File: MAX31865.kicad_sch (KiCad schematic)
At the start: 25 parts, among them U1 MAX31865, U2 MIC5225-3.3, X1 3.5mm, X2 3.5mm

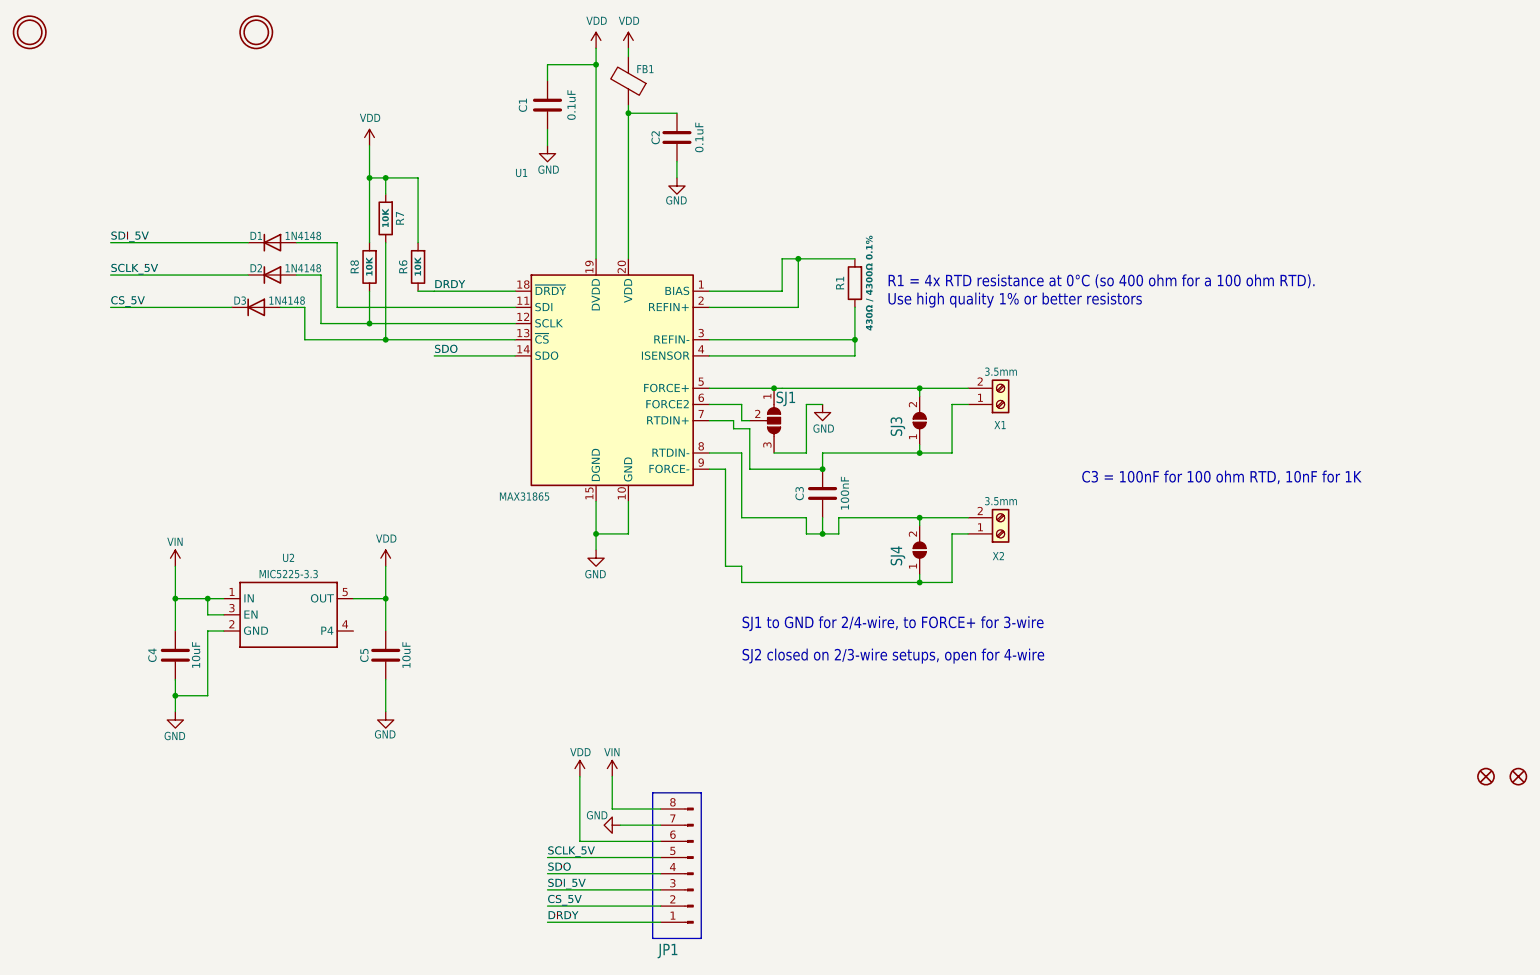
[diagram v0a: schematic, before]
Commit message: fixed routing + added BOM info
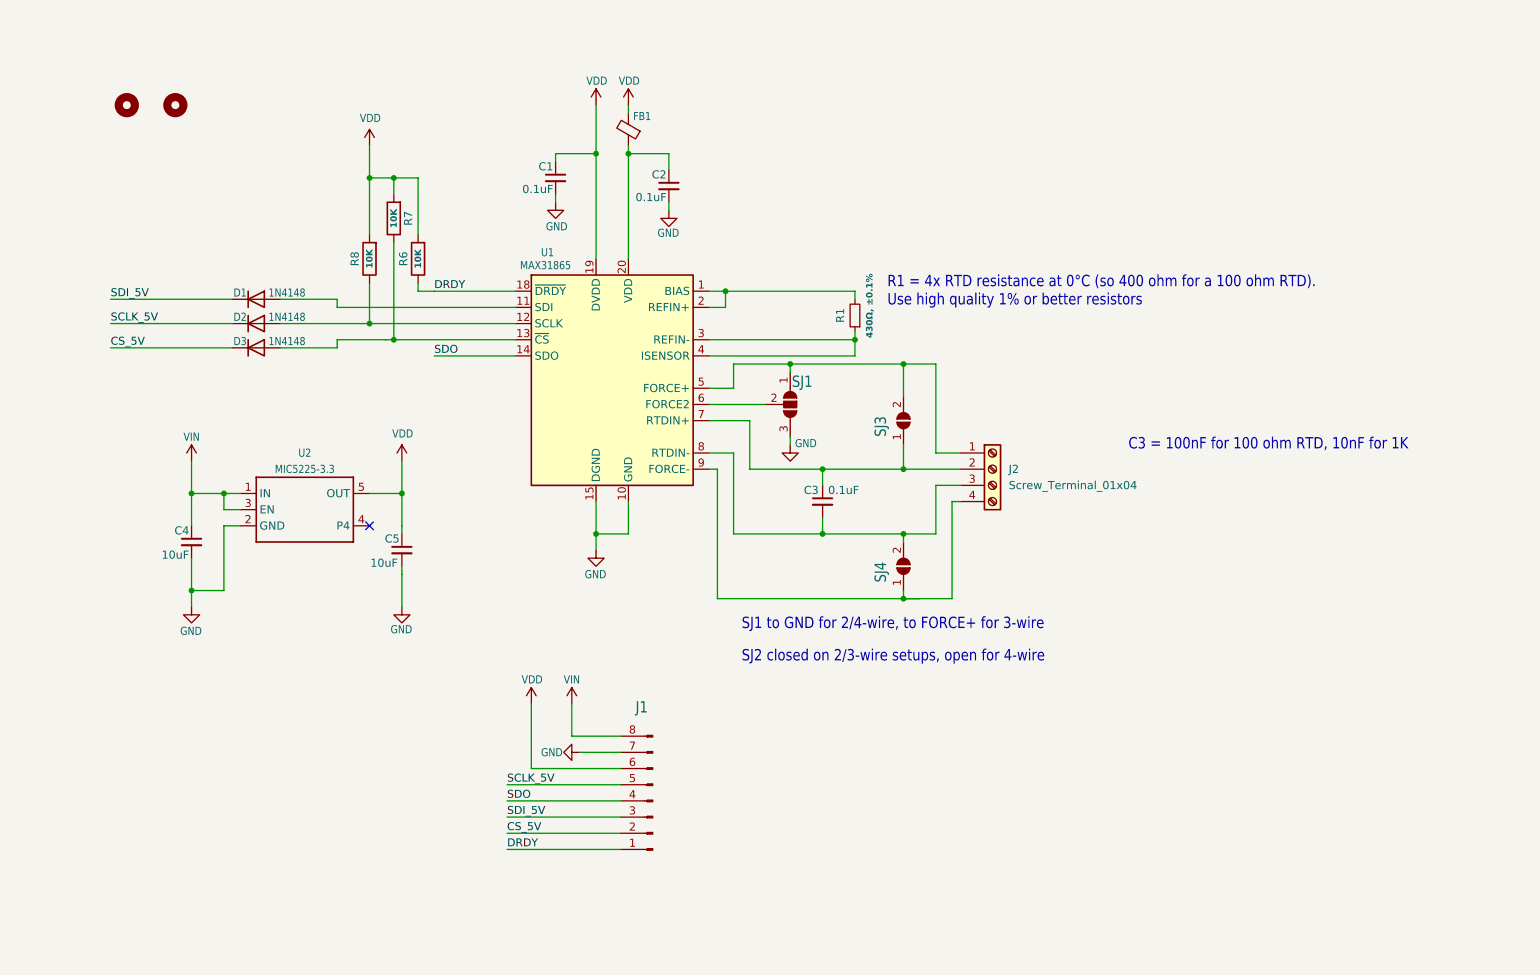
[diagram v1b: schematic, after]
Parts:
- removed FID1, FID2: FIDUCIAL{dblquote}{dblquote}, Fiducial:Fiducial_1mm_Mask2mm, symbol MAX31865-eagle-import:FIDUCIAL{dblquote}{dblquote}
- removed X1, X2: 3.5mm, TerminalBlock_4Ucon:TerminalBlock_4Ucon_1x02_P3.50mm_Horizontal, symbol Connector:Screw_Terminal_01x02
- added J2: Screw_Terminal_01x04, TerminalBlock_4Ucon:TerminalBlock_4Ucon_1x04_P3.50mm_Horizontal, symbol Connector:Screw_Terminal_01x04
- C1, C2: symbol Device:C -> Device:C_Small; MPN (none) -> /; Manufacturer (none) -> /; SPN (none) -> GPC0805104; Supplier (none) -> Eurocircuits
- C3: value 100nF -> 0.1uF; symbol Device:C -> Device:C_Small; MPN (none) -> /; Manufacturer (none) -> /; SPN (none) -> GPC0805104; Supplier (none) -> Eurocircuits
- C4, C5: symbol Device:C -> Device:C_Small; Component package type (none) -> C_0805; MPN (none) -> /; Manufacturer (none) -> /; SPN (none) -> GPC0805106-16; Supplier (none) -> Eurocircuits
- D1, D2, D3: Component package type (none) -> SOD-323; MPN (none) -> 1N4148WX-TP; Manufacturer (none) -> Micro Commercial Co; SPN (none) -> 1N4148WXTPMSTR-ND; Supplier (none) -> DigiKey
- FB1: footprint MAX31865:0805-NO -> Inductor_SMD:L_0805_2012Metric; symbol Device:FerriteBead -> Device:FerriteBead_Small; MPN (none) -> LI0805G201R-10; Manufacturer (none) -> Laird-Signal Integrity Products; SPN (none) -> 240-2549-2-ND; Supplier (none) -> DigiKey
- J1: renamed from JP1; value HEADER-1X870MIL -> connector; footprint Connector_PinHeader_1.00mm:PinHeader_1x08_P1.00mm_Vertical -> Connector_PinHeader_2.54mm:PinHeader_1x08_P2.54mm_Vertical; Component package type (none) -> /; MPN (none) -> TSW-108-09-G-S; Manufacturer (none) -> Samtec Inc.; SPN (none) -> SAM12332-ND; Supplier (none) -> DigiKey
- R1: value 430Ω / 4300Ω 0.1% -> 430Ω, ±0.1%; symbol Device:R -> Device:R_Small; MPN (none) -> /; Manufacturer (none) -> /; SPN (none) -> GPR0805430R; Supplier (none) -> Eurocircuits
- R6, R7, R8: MPN (none) -> /; Manufacturer (none) -> /; SPN (none) -> GPR080510K; Supplier (none) -> Eurocircuits
- SJ1: footprint MAX31865:SOLDERJUMPER_2WAY_OPEN_NOPASTE -> Jumper:SolderJumper-3_P1.3mm_Open_Pad1.0x1.5mm; now left out of the parts list
- SJ3, SJ4: now left out of the parts list
- U$18, U$19: footprint MountingHole:MountingHole_2.5mm -> MountingHole:MountingHole_2.2mm_M2_ISO7380; symbol MAX31865-eagle-import:MOUNTINGHOLE2.5 -> Mechanical:MountingHole; now left out of the parts list
- U1: Component package type (none) -> 20-TQFN (5x5); MPN (none) -> MAX31865ATP+; Manufacturer (none) -> Analog Devices Inc./Maxim Integrated; SPN (none) -> MAX31865ATP+-ND; Supplier (none) -> DigiKey
- U2: Component package type (none) -> SOT-235; MPN (none) -> MIC5225-3.3YM5-TR; Manufacturer (none) -> Microchip Technology; SPN (none) -> 576-2980-2-ND; Supplier (none) -> DigiKey
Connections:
- net at SJ4.1 (A), U1.9 (FORCE-): now also J2.4 (Pin_4)
- net at C3.2, SJ4.2 (B), U1.8 (RTDIN-): now also J2.3 (Pin_3)
- net at C3.1, SJ3.1 (A), U1.7 (RTDIN+): now also J2.2 (Pin_2)
- net at SJ1.1 (A), SJ3.2 (B), U1.5 (FORCE+): now also J2.1 (Pin_1)
- no-connect marks 0 -> 1
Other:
- moved on the sheet: C1, C2, C3, C4, C5, D1, D2, D3, FB1, J1, R1, R6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

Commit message: removed imported library
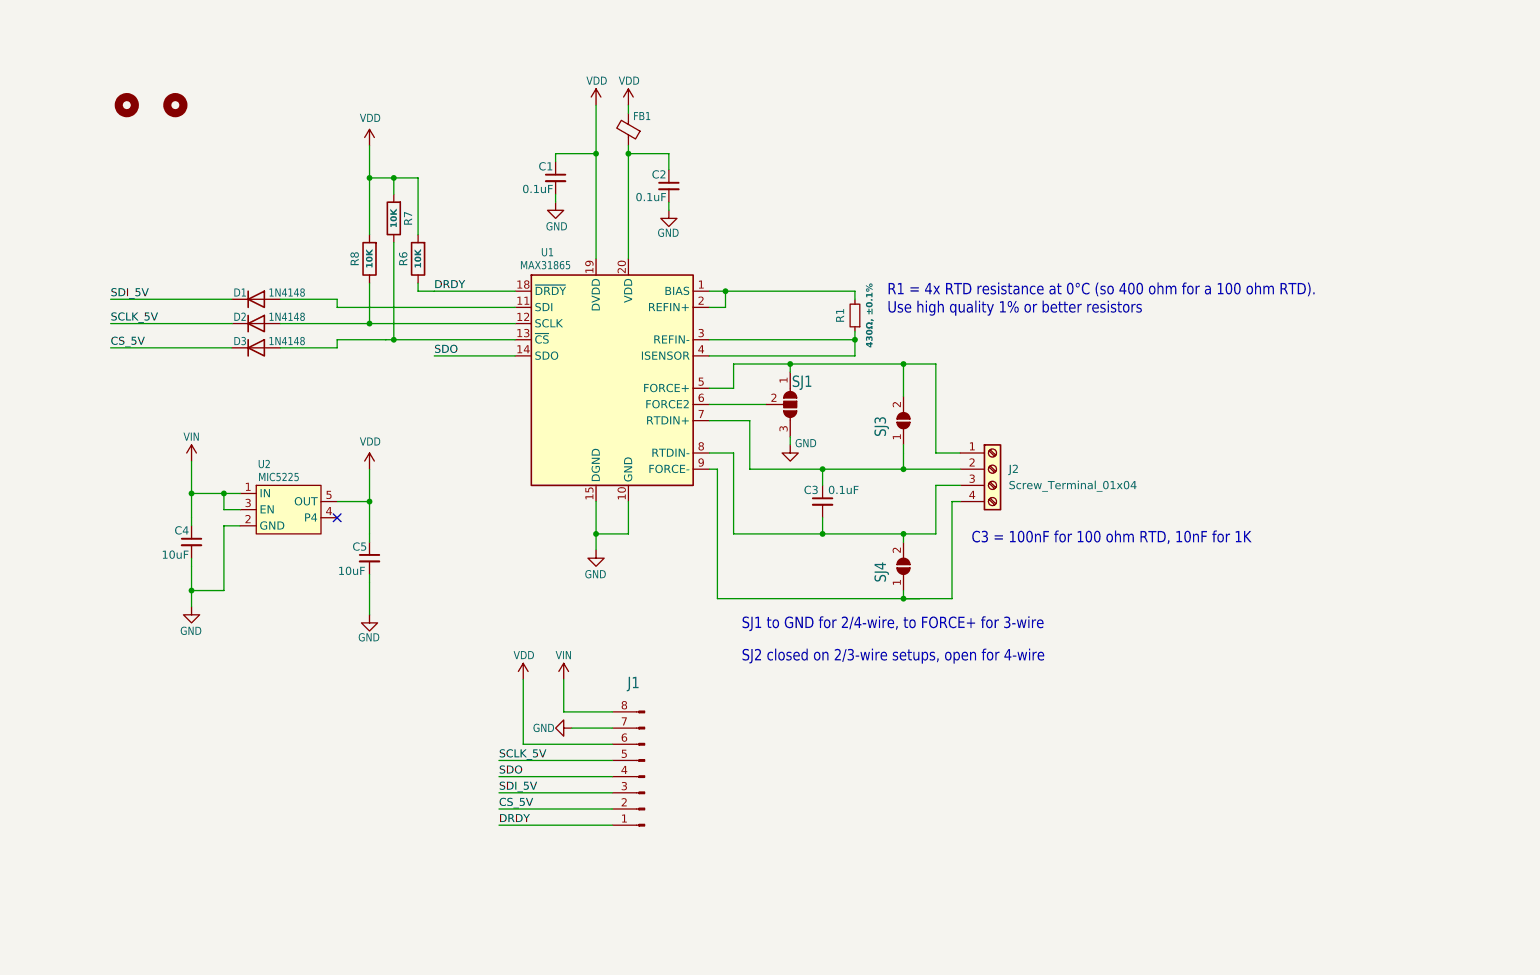
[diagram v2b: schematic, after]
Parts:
- U2: value MIC5225-3.3 -> MIC5225; symbol VREG_SOT23-5:VREG_SOT23-5 -> external_library:MIC5225
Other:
- moved on the sheet: C5, J1

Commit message: improved routing
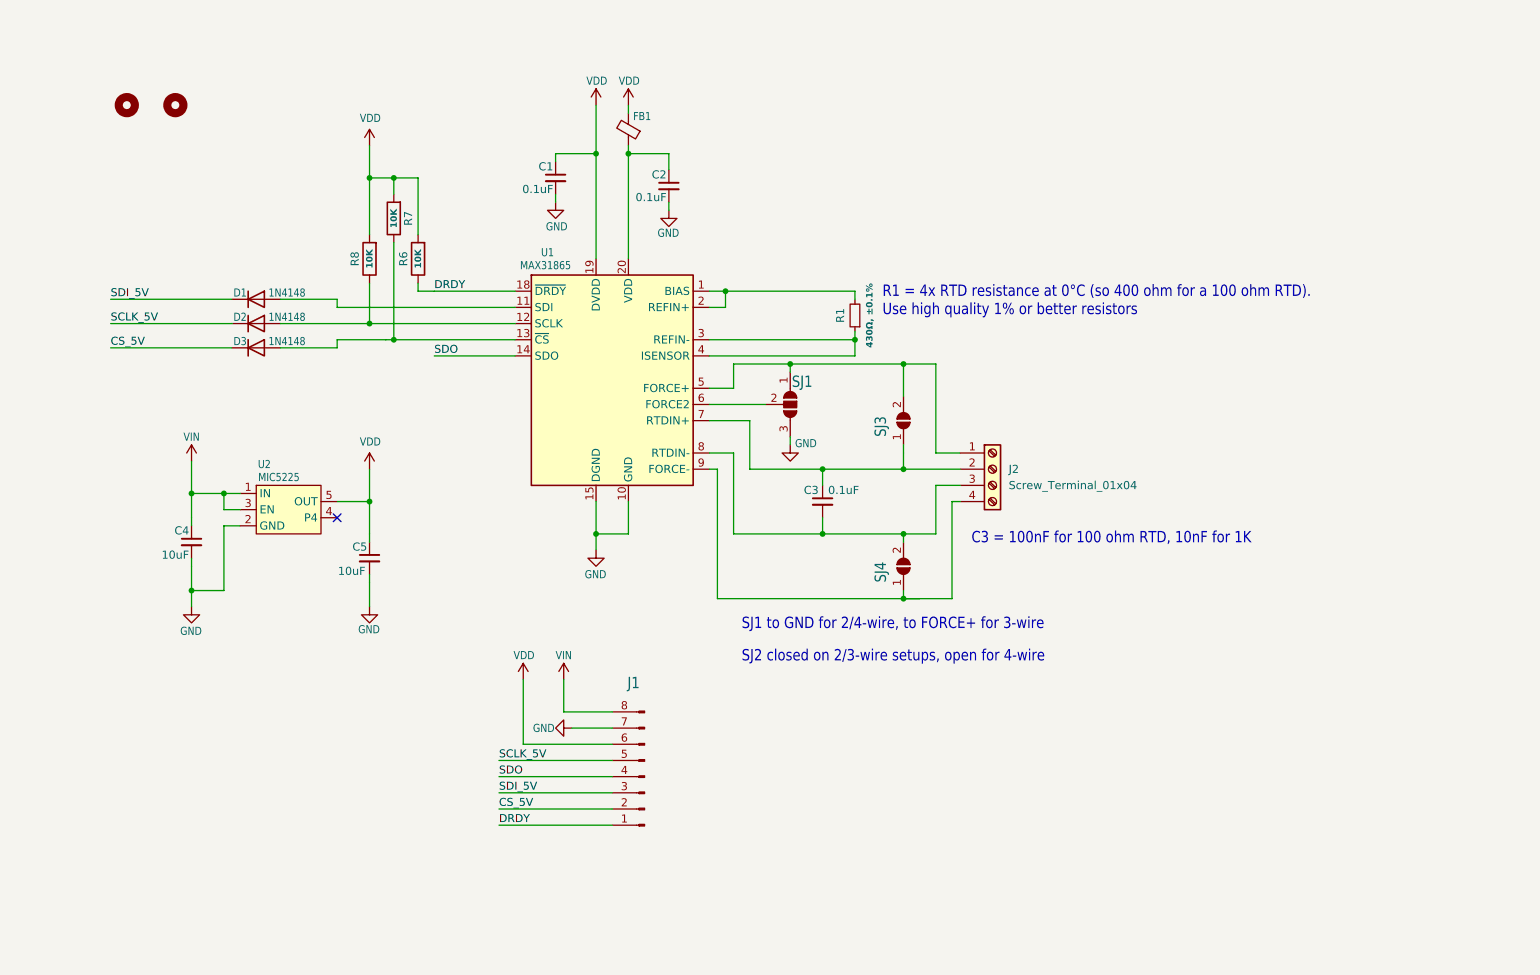
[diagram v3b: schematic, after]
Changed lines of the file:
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@@
 	(wire
 		(pts
-			(xy 91.44 127) (xy 91.44 132.08)
+			(xy 91.44 127) (xy 91.44 130.81)
 		)
 		(stroke
@@
 	(text "R1 = 4x RTD resistance at 0°C (so 400 ohm for a 100 ohm RTD).\nUse high quality 1% or better resistors"
 		(exclude_from_sim no)
-		(at 172.72 85.09 0)
+		(at 171.958 85.344 0)
 		(effects
 			(font
@@
 	(symbol
 		(lib_id "power:GND")
-		(at 91.44 132.08 0)
+		(at 91.44 130.81 0)
 		(unit 1)
 		(exclude_from_sim no)
@@
 		(dnp no)
 		(property "Reference" "#U$012"
-			(at 91.44 132.08 0)
+			(at 91.44 130.81 0)
 			(effects
 				(font
@@
 		)
 		(property "Value" "GND"
-			(at 89.662 136.398 0)
+			(at 89.662 135.128 0)
 			(effects
 				(font
@@
 		)
 		(property "Footprint" ""
-			(at 91.44 132.08 0)
+			(at 91.44 130.81 0)
 			(effects
 				(font
@@
 		)
 		(property "Datasheet" ""
-			(at 91.44 132.08 0)
+			(at 91.44 130.81 0)
 			(effects
 				(font
@@
 		)
 		(property "Description" "Power symbol creates a global label with name \"GND\" , ground"
-			(at 91.44 132.08 0)
-			(effects
-				(font
+			(at 91.44 130.81 0)
+			(effects
+				(font

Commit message: updated solder jumper
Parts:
- removed SJ1: SOLDERJUMPER_2WAY, Jumper:SolderJumper-3_P1.3mm_Open_Pad1.0x1.5mm, symbol Jumper:SolderJumper_3_Open
- added JP1: SolderJumper_3_Bridged12, Jumper:SolderJumper-3_P1.3mm_Bridged12_Pad1.0x1.5mm, symbol Jumper:SolderJumper_3_Bridged12
- renumbered SJ3 to JP2, SJ4 to JP3
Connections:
- net GND: now also JP1.1 (A)
- net at J2.1 (Pin_1), JP2.2 (B), U1.5 (FORCE+): now also JP1.3 (B)
- net at U1.6 (FORCE2): now also JP1.2 (C)
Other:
- note added: "JP1 to GND for 2/4-wire, to FORCE+ for 3-wire"
- note added: "JP2 closed on 2/3-wire setups, open for 4-wire"
- note removed: "SJ1 to GND for 2/4-wire, to FORCE+ for 3-wire"
- note removed: "SJ2 closed on 2/3-wire setups, open for 4-wire"
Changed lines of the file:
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@@
 		)
 	)
-	(text "SJ1 to GND for 2/4-wire, to FORCE+ for 3-wire"
+	(text "JP1 to GND for 2/4-wire, to FORCE+ for 3-wire"
 		(exclude_from_sim no)
 		(at 149.86 134.62 0)
@@
 		)
 	)
-	(text "SJ2 closed on 2/3-wire setups, open for 4-wire"
+	(text "JP2 closed on 2/3-wire setups, open for 4-wire"
 		(exclude_from_sim no)
 		(at 149.86 139.7 0)
@@
 		(on_board yes)
 		(dnp no)
-		(property "Reference" "SJ4"
-			(at 172.72 127 0)
-			(effects
-				(font
-					(size 1.778 1.5113)
+		(property "Reference" "JP3"
+			(at 173.736 123.698 90)
+			(effects
+				(font
+					(size 1.27 1.27)
 				)
 				(justify left bottom)
@@
 			(project "MAX31865"
 				(path "/7d3dfe06-ad22-4135-8721-3b06d69e4560"
-					(reference "SJ4")
+					(reference "JP3")
 					(unit 1)
 				)
@@
 		(on_board yes)
 		(dnp no)
-		(property "Reference" "SJ3"
-			(at 172.72 104.14 0)
-			(effects
-				(font
-					(size 1.778 1.5113)
+		(property "Reference" "JP2"
+			(at 173.482 100.838 90)
+			(effects
+				(font
+					(size 1.27 1.27)
 				)
 				(justify left bottom)
@@
 			(project "MAX31865"
 				(path "/7d3dfe06-ad22-4135-8721-3b06d69e4560"
-					(reference "SJ3")
+					(reference "JP2")
 					(unit 1)
 				)
@@
 	)
 	(symbol
-		(lib_id "Jumper:SolderJumper_3_Open")
-		(at 157.48 99.06 270)
-		(unit 1)
-		(exclude_from_sim no)
-		(in_bom no)
-		(on_board yes)
-		(dnp no)
-		(property "Reference" "SJ1"
-			(at 157.734 96.52 90)
-			(effects
-				(font
-					(size 1.778 1.5113)
-				)
-				(justify left bottom)
-			)
-		)
-		(property "Value" "SOLDERJUMPER_2WAY"
-			(at 151.13 93.98 0)
-			(effects
-				(font
-					(size 1.778 1.5113)
-				)
-				(justify left bottom)
-				(hide yes)
-			)
-		)
-		(property "Footprint" "Jumper:SolderJumper-3_P1.3mm_Open_Pad1.0x1.5mm"
-			(at 157.48 99.06 0)
-			(effects
-				(font
-					(size 1.27 1.27)
-				)
-				(hide yes)
-			)
-		)
-		(property "Datasheet" "~"
-			(at 157.48 99.06 0)
-			(effects
-				(font
-					(size 1.27 1.27)
-				)
-				(hide yes)
-			)
-		)
-		(property "Description" "Solder Jumper, 3-pole, open"
-			(at 157.48 99.06 0)
-			(effects
-				(font
-					(size 1.27 1.27)
-				)
-				(hide yes)
-			)
-		)
-		(property "Component package type" ""
-			(at 157.48 99.06 0)
-			(effects
-				(font
-					(size 1.27 1.27)
-				)
-				(hide yes)
-			)
-		)
-		(property "MPN" ""
-			(at 157.48 99.06 0)
-			(effects
-				(font
-					(size 1.27 1.27)
-				)
-				(hide yes)
-			)
-		)
-		(property "Manufacturer" ""
-			(at 157.48 99.06 0)
-			(effects
-				(font
-					(size 1.27 1.27)
-				)
-				(hide yes)
-			)
-		)
-		(property "SPN" ""
-			(at 157.48 99.06 0)
-			(effects
-				(font
-					(size 1.27 1.27)
-				)
-				(hide yes)
-			)
-		)
-		(property "Supplier" ""
-			(at 157.48 99.06 0)
-			(effects
-				(font
-					(size 1.27 1.27)
-				)
-				(hide yes)
-			)
-		)
-		(pin "1"
-		)
-		(pin "2"
-		)
-		(pin "3"
-		)
-		(instances
-			(project "MAX31865"
-				(path "/7d3dfe06-ad22-4135-8721-3b06d69e4560"
-					(reference "SJ1")
-					(unit 1)
-				)
-			)
-		)
-	)
-	(symbol
 		(lib_id "power:GND")
 		(at 123.19 149.86 270)
@@
 					(unit 1)
 				)
+			)
+		)
+	)
+	(symbol
+		(lib_id "Jumper:SolderJumper_3_Bridged12")
+		(at 157.48 99.06 270)
+		(mirror x)
+		(unit 1)
+		(exclude_from_sim yes)
+		(in_bom no)
+		(on_board yes)
+		(dnp no)
+		(property "Reference" "JP1"
+			(at 159.004 99.06 90)
+			(effects
+				(font
+					(size 1.27 1.27)
+				)
+				(justify left)
+			)
+		)
+		(property "Value" "SolderJumper_3_Bridged12"
+			(at 160.02 97.7901 90)
+			(effects
+				(font
+					(size 1.27 1.27)
+				)
+				(justify left)
+				(hide yes)
+			)
+		)
+		(property "Footprint" "Jumper:SolderJumper-3_P1.3mm_Bridged12_Pad1.0x1.5mm"
+			(at 157.48 99.06 0)
+			(effects
+				(font
+					(size 1.27 1.27)
+				)
+				(hide yes)
+			)
+		)
+		(property "Datasheet" "~"
+			(at 157.48 99.06 0)
+			(effects
+				(font
+					(size 1.27 1.27)
+				)
+				(hide yes)
+			)
+		)
+		(property "Description" "3-pole Solder Jumper, pins 1+2 closed/bridged"
+			(at 157.48 99.06 0)
+			(effects
+				(font
+					(size 1.27 1.27)
+				)
+				(hide yes)
+			)
+		)
+		(pin "2"
+		)
+		(pin "1"
+		)
+		(pin "3"
+		)
+		(instances
+			(project "MAX31865"
+				(path "/7d3dfe06-ad22-4135-8721-3b06d69e4560"
+					(reference "JP1")
+					(unit 1)
+				)

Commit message: fixed connection mistake
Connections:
- net DRDY: no longer R6.1
- net at D1.2 (A), U1.11 (SDI): now also R6.1
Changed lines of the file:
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@@
+	)
+	(junction
+		(at 99.06 83.82)
+		(diameter 0)
+		(color 0 0 0 0)
 	)
 	(junction
@@
 	(wire
 		(pts
+			(xy 99.06 83.82) (xy 114.3 83.82)
+		)
+		(stroke
+			(width 0.1524)
+			(type solid)
+		)
+	)
+	(wire
+		(pts
 			(xy 184.15 106.68) (xy 180.34 106.68)
 		)
@@
 	(wire
 		(pts
-			(xy 99.06 81.28) (xy 101.6 81.28)
-		)
-		(stroke
-			(width 0)
-			(type default)
-		)
-	)
-	(wire
-		(pts
 			(xy 132.08 52.07) (xy 132.08 53.34)
 		)
@@
 	(wire
 		(pts
-			(xy 99.06 81.28) (xy 99.06 80.01)
-		)
-		(stroke
-			(width 0)
-			(type default)
-		)
-	)
-	(wire
-		(pts
 			(xy 175.26 92.71) (xy 180.34 92.71)
 		)
@@
 	(wire
 		(pts
-			(xy 86.36 83.82) (xy 114.3 83.82)
+			(xy 86.36 83.82) (xy 99.06 83.82)
 		)
 		(stroke
@@
 		)
 	)
+	(wire
+		(pts
+			(xy 99.06 80.01) (xy 99.06 83.82)
+		)
+		(stroke
+			(width 0)
+			(type default)
+		)
+	)
